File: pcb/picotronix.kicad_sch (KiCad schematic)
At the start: 25 parts, among them J1 Conn_02x04_Odd_Even, J2 Conn_02x04_Odd_Even, J3 DEBUG, J4 DB25_Male, U1 Pico, U2 TXS0104PW, U3 DAC7562SDGST, U4 TL074

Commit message: revised
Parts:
- removed C3, C4: C, Capacitor_SMD:C_0603_1608Metric_Pad1.08x0.95mm_HandSolder, symbol Device:C
- removed JP1: filter_bypass, Jumper:SolderJumper-2_P1.3mm_Open_Pad1.0x1.5mm, symbol Jumper:SolderJumper_2_Open
- removed R2, R3: R_US, Resistor_SMD:R_0603_1608Metric_Pad0.98x0.95mm_HandSolder, symbol Device:R_US
- removed RV1: Z Trim, Potentiometer_SMD:Potentiometer_Bourns_TC33X_Vertical, symbol Device:R_Potentiometer_Trim_US
- removed RV2: X Trim, Potentiometer_SMD:Potentiometer_Bourns_TC33X_Vertical, symbol Device:R_Potentiometer_Trim_US
- removed RV3: Y Trim, Potentiometer_SMD:Potentiometer_Bourns_TC33X_Vertical, symbol Device:R_Potentiometer_Trim_US
- removed U4: TL074, Package_SO:SOIC-14_3.9x8.7mm_P1.27mm, symbol Amplifier_Operational:TL074
- added R2: (no value), symbol Device:R
- added RN1, RN3: (no value), symbol Device:R_Pack04_Split
- added RN2: (no value), symbol Device:R_Pack04
- added RV1, RV2, RV3: (no value), symbol Device:R_Potentiometer_Trim
- added U4: (no value), symbol picotronix:ADA4891-3
- C1, C2, C5: value 0.1u -> (none); footprint Capacitor_SMD:C_0603_1608Metric_Pad1.08x0.95mm_HandSolder -> (none)
- C6: value 1u -> (none); footprint Capacitor_SMD:C_0603_1608Metric_Pad1.08x0.95mm_HandSolder -> (none)
- H1, H2, H3, H4: value MountingHole -> (none); footprint MountingHole:MountingHole_3.2mm_M3 -> (none)
- J1, J2: value Conn_02x04_Odd_Even -> (none); footprint Connector_PinSocket_2.54mm:PinSocket_2x04_P2.54mm_Vertical -> (none)
- J3: value DEBUG -> (none); footprint Connector_PinHeader_2.54mm:PinHeader_1x03_P2.54mm_Vertical -> (none)
- J4: value DB25_Male -> (none); footprint Connector_Dsub:DSUB-25_Male_Horizontal_P2.77x2.54mm_EdgePinOffset9.40mm -> (none)
- R1: value 10k -> (none); footprint Resistor_SMD:R_0603_1608Metric_Pad0.98x0.95mm_HandSolder -> (none); symbol Device:R_US -> Device:R
- U1: value Pico -> (none); footprint picotronix:RPi_Pico_SMD_TH -> (none)
- U2: value TXS0104PW -> (none); footprint Package_SO:TSSOP-14_4.4x5mm_P0.65mm -> (none); symbol picotronix:TXS0104PW -> picotronix:LSF0204DPWR; Digikey_PN (none) -> 296-40400-1-ND
- U3: value DAC7562SDGST -> (none); footprint Package_SO:VSSOP-10_3x3mm_P0.5mm -> (none); Digikey_PN (none) -> 296-38921-1-ND
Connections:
- net +5V: now also U4.4 (+V_{s})
- net GND: now also R2.1, RV3.3, U4.11 (-V_{s})
- net X_OUTPUT: now also RN2.1 (R1.1)
- net Y_OUTPUT: now also RN2.2 (R2.1)
- net Z_OUTPUT: now also RN2.3 (R3.1)
- net at U3.1 (V_{OUT}A): now also RV1.1
- net at U3.2 (V_{OUT}B): now also RV2.1
- net z_pwm: no longer names the net of U1.21 (GPIO16)
- new net: RN1.3 (R3.1), RN3.6 (R3.2), RN3.7 (R2.2)
- new net: RV2.2, U4.12 (+)
- new net: RN2.8 (R1.2), U4.13 (-), U4.15
- new net: RN2.6 (R3.2), U4.8, U4.9 (-)
- new net: RN2.7 (R2.2), U4.6 (-), U4.7
- new net: RN1.4 (R4.1), RN3.3 (R3.1), RV3.1
- new net: RN1.2 (R2.1), RN3.1 (R1.1), RN3.2 (R2.1)
- new net: R2.2, RN1.1 (R1.1), RN3.8 (R1.2)
- new net: RV3.2, U4.10 (+)
- new net: RV1.2, U4.5 (+)
- no-connect marks 20 -> 24
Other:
- note added: "extra gpio for later expansion"
- note added: "snub resistors to reduce peaking"
- note removed: "trim pots allow for ranging from 0-3.3v maximum."
- note removed: "z-axis pwm filter"
- moved on the sheet: C1, C2, C5, C6, J1, J2, U2

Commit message: update pcb
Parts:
- added TP? (x3): (no value), symbol Connector:TestPoint
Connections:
- net GND: now also RV1.3, RV2.3
- net X_OUTPUT: now also TP?.1
- net Y_OUTPUT: now also TP?.1
- net Z_OUTPUT: now also TP?.1
- net erase_interval_l: now also U1.32 (GPIO27_ADC1); no longer U1.31 (GPIO26_ADC0)
- net erase_l: now also U1.29 (GPIO22); no longer U1.27 (GPIO21)
- net non_store_l: now also U1.31 (GPIO26_ADC0); no longer U1.29 (GPIO22)
- net var_bright_l: now also U1.34 (GPIO28_ADC2); no longer U1.32 (GPIO27_ADC1)
- net ~{CS}: now also U1.27 (GPIO21); no longer U1.22 (GPIO17)
- net z_{3}: now reaches RN1.6 (R3.2)
- net z_{3}: now also U1.21 (GPIO16)
- net z_{1}: now reaches U1.19 (GPIO14)
- net z_{1}: now also RN1.8 (R1.2)
- net z_{2}: now reaches U1.20 (GPIO15)
- net z_{2}: now also RN1.7 (R2.2)
- net z_{4}: now reaches RN1.5 (R4.2)
- net z_{4}: now also U1.22 (GPIO17)
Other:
- note added: "r2r z-axis dac"
- moved on the sheet: RV1, RV2, U3, U4A, U4B

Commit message: update pcb
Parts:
- C1, C2, C5: value (none) -> 0.1u; footprint (none) -> Capacitor_SMD:C_0603_1608Metric_Pad1.08x0.95mm_HandSolder
- C6: value (none) -> 1u; footprint (none) -> Capacitor_SMD:C_0603_1608Metric_Pad1.08x0.95mm_HandSolder
- H1, H2, H3, H4: value (none) -> MountingHole; footprint (none) -> MountingHole:MountingHole_3.2mm_M3
- J1, J2: value (none) -> Conn_02x04_Odd_Even; footprint (none) -> Connector_PinSocket_2.54mm:PinSocket_2x04_P2.54mm_Vertical
- J3: value (none) -> DEBUG; footprint (none) -> Connector_PinHeader_2.54mm:PinHeader_1x03_P2.54mm_Vertical
- J4: value (none) -> DB25_Male; footprint (none) -> Connector_Dsub:DSUB-25_Male_Horizontal_P2.77x2.54mm_EdgePinOffset9.40mm
- R1, R2: value (none) -> 10k; footprint (none) -> Resistor_SMD:R_0603_1608Metric_Pad0.98x0.95mm_HandSolder
- RN1: value (none) -> 10k; footprint (none) -> Resistor_SMD:R_Array_Convex_4x1206
- RN2: value (none) -> 470; footprint (none) -> Resistor_SMD:R_Array_Convex_4x1206
- RN3: value (none) -> 4.99k; footprint (none) -> Resistor_SMD:R_Array_Convex_4x1206
- RV1, RV2, RV3: value (none) -> 20k; footprint (none) -> Potentiometer_SMD:Potentiometer_Bourns_TC33X_Vertical
- TP1: renamed from TP?; value (none) -> Z Test
- TP2: renamed from TP?; value (none) -> Y Test
- TP3: renamed from TP?; value (none) -> X test
- U1: value (none) -> Pico; footprint (none) -> picotronix:RPi_Pico_SMD_TH
- U2: value (none) -> LSF0204DPWR; footprint (none) -> Package_SO:TSSOP-14_4.4x5mm_P0.65mm
- U3: value (none) -> DAC7562SDGST; footprint (none) -> Package_SO:VSSOP-10_3x3mm_P0.5mm
- U4: value (none) -> ADA4891-3; footprint (none) -> Package_SO:TSSOP-14_4.4x5mm_P0.65mm

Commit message: pcb rev2 routed
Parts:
- removed J2: Conn_02x04_Odd_Even, Connector_PinSocket_2.54mm:PinSocket_2x04_P2.54mm_Vertical, symbol Connector_Generic:Conn_02x04_Odd_Even
- removed J3: DEBUG, Connector_PinHeader_2.54mm:PinHeader_1x03_P2.54mm_Vertical, symbol Connector:Conn_01x03_Male
- added C1, C10, C11, C2, C9: 0.1u, Capacitor_SMD:C_0603_1608Metric_Pad1.08x0.95mm_HandSolder, symbol Device:C_Small
- added C7, C8: 1u, Capacitor_SMD:C_0603_1608Metric_Pad1.08x0.95mm_HandSolder, symbol Device:C_Small
- added J1: AudioJack3_Ground, Connector_Audio:Jack_3.5mm_CUI_SJ-3524-SMT_Horizontal, symbol Connector:AudioJack3_Ground
- added J3: DEBUG, Connector_PinHeader_2.54mm:PinHeader_2x03_P2.54mm_Vertical, symbol Connector_Generic:Conn_02x03_Odd_Even
- added JP1: FMT_SET, Jumper:SolderJumper-2_P1.3mm_Open_TrianglePad1.0x1.5mm, symbol Jumper:SolderJumper_2_Open
- added JP2: MD1_SET, Jumper:SolderJumper-2_P1.3mm_Open_TrianglePad1.0x1.5mm, symbol Jumper:SolderJumper_2_Open
- added JP3: MD0_SET, Jumper:SolderJumper-2_P1.3mm_Open_TrianglePad1.0x1.5mm, symbol Jumper:SolderJumper_2_Open
- added R1: 10k, Resistor_SMD:R_0603_1608Metric_Pad0.98x0.95mm_HandSolder, symbol Device:R
- added SW1: BTN0, Button_Switch_SMD:SW_SPST_TL3305A, symbol Switch:SW_Push
- added SW2: BTN1, Button_Switch_SMD:SW_SPST_TL3305A, symbol Switch:SW_Push
- added SW3: RESET, Button_Switch_SMD:SW_SPST_TL3305A, symbol Switch:SW_Push
- added U5: W25Q128JVS, Package_SO:SOIC-8_5.23x5.23mm_P1.27mm, symbol Memory_Flash:W25Q128JVS
- added U6: PCM1808, Package_SO:TSSOP-14_4.4x5mm_P0.65mm, symbol picotronix:PCM1808
- J2: renamed from J1; value Conn_02x04_Odd_Even -> ESP-01 Connector
- J4: footprint Connector_Dsub:DSUB-25_Male_Horizontal_P2.77x2.54mm_EdgePinOffset9.40mm -> Connector_Dsub:DSUB-25_Male_Horizontal_P2.77x2.84mm_EdgePinOffset9.90mm_Housed_MountingHolesOffset11.32mm; symbol Connector:DB25_Male -> Connector:DB25_Male_MountingHoles
- TP1, TP2, TP3: footprint (none) -> TestPoint:TestPoint_Pad_2.0x2.0mm
- U3: value DAC7562SDGST -> AD5663R; footprint Package_SO:VSSOP-10_3x3mm_P0.5mm -> Package_SO:MSOP-10_3x3mm_P0.5mm; symbol picotronix:DAC7562SDGST -> picotronix:AD5663R; Digikey_PN 296-38921-1-ND -> AD5623RBRMZ-5REEL7CT-ND
- renumbered C1 to C3, C2 to C4, R1 to R2, R2 to R3, RN3 to RN2, RN2 to RN3, RV3 to RV1, RV1 to RV2, RV2 to RV3
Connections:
- net gpio6 is gone; now on net erase_interval_l: U1.9 (GPIO6)
- net gpio7 is gone; now on net erase_l: U1.10 (GPIO7)
- net +3V3: now also C1.1, C11.1, C9.1, JP1.2 (B), JP2.2 (B), JP3.2 (B), R1.1, U5.8 (VCC), U6.4 (V_{DD})
- net +5V: now also C10.1, U6.3 (V_{CC})
- net GND: now also J4.0 (PAD), C1.2, C10.2, C11.2, C2.2, C9.2, J1.G, J1.T, J3.5 (Pin_5), J3.6 (Pin_6), SW1.1, SW2.1, SW3.2, U5.4 (GND), U6.2 (AGND), U6.5 (DGND)
- net XY_FLUSH: now also U1.21 (GPIO16); no longer U1.26 (GPIO20)
- net erase_interval_l: no longer U1.32 (GPIO27_ADC1)
- net erase_l: no longer U1.29 (GPIO22)
- net non_store_l: now also U1.26 (GPIO20); no longer U1.31 (GPIO26_ADC0)
- net z_{1}: now also U1.16 (GPIO12); no longer U1.19 (GPIO14)
- net z_{2}: now also U1.17 (GPIO13); no longer U1.20 (GPIO15)
- net z_{3}: now also U1.19 (GPIO14); no longer U1.21 (GPIO16)
- net z_{4}: now also U1.20 (GPIO15); no longer U1.22 (GPIO17)
- net ~{CS}: now also U1.22 (GPIO17); no longer U1.27 (GPIO21)
- net at RN1.3 (R3.1), RN2.6 (R3.2): now also RN2.2 (R2.1); no longer RN2.7 (R2.2)
- net at RN1.2 (R2.1), RN2.1 (R1.1): now also RN2.7 (R2.2); no longer RN2.2 (R2.1)
- net at U1.30 (RUN): now also SW3.1
- net at U1.41 (SWCLK): now also J3.3 (Pin_3)
- net at U1.43 (SWDIO): now also J3.1 (Pin_1)
- net gpio0 renamed UART0_RX
- net UART0_RX: now also U1.2 (GPIO1); no longer U1.1 (GPIO0)
- net gpio1: no longer names the net of J2.3 (Pin_3)
- net gpio1: no longer U1.2 (GPIO1)
- net gpio10 renamed FLASH_SCK
- net FLASH_SCK: now also U5.6 (CLK)
- net gpio11 renamed FLASH_MOSI
- net FLASH_MOSI: now also U5.5 (DI(IO0))
- net gpio2: no longer names the net of U1.4 (GPIO2)
- net gpio2: now also SW1.2; no longer J2.4 (Pin_4)
- net gpio3: no longer names the net of J2.5 (Pin_5)
- net gpio3: no longer U1.5 (GPIO3)
- net gpio4: no longer names the net of J2.6 (Pin_6)
- net gpio4: no longer U1.6 (GPIO4)
- net gpio5 renamed UART0_TX
- net UART0_TX: now also U1.1 (GPIO0); no longer U1.7 (GPIO5)
- net gpio8 renamed FLASH_MISO
- net FLASH_MISO: now also U5.2 (DO(IO1))
- net gpio9 renamed FLASH_CS
- net FLASH_CS: now also U5.1 (~{CS})
- new net: JP2.1 (A), U6.11 (MD1)
- new net: JP3.1 (A), U6.10 (MD0)
- new net: SW2.2, U1.5 (GPIO3)
- new net: C2.1, U6.1 (V_{REF})
- new net: JP1.1 (A), U6.12 (FMT)
- new net: C7.1, U6.13 (V_{IN}L)
- new net: C8.1, U6.14 (V_{IN}R)
- new net: C7.2, J1.S
- new net: C8.2, J1.R
- new net dbg_rx: J3.2 (Pin_2), U1.7 (GPIO5)
- new net dbg_tx: J3.4 (Pin_4), U1.6 (GPIO4)
- new net esp_en: J2.4 (Pin_4), R1.2
- new net i2s_bck: U1.29 (GPIO22), U6.8 (BCK)
- new net i2s_dout: U1.31 (GPIO26_ADC0), U6.9 (DOUT)
- new net i2s_lrclk: U1.32 (GPIO27_ADC1), U6.7 (LRCK)
- new net i2s_mclk: U1.27 (GPIO21), U6.6 (SCKI)
- no-connect marks 24 -> 28
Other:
- note added: "audio input for reactive displays"
- note added: "esp-01 header for network connectivity"
- note added: "solder jumpers to set mode (internal pulldown)"
- note removed: "expansion ports are designed to be ESP-01 compatible"
- note removed: "extra gpio for later expansion"
- company: (none) -> Saji Champlin
- title: (none) -> Picotronix Main Board
- moved on the sheet: C3, C4, C5, C6, H1, H2, H3, H4, J2, R2, R3, RN1A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

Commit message: pcb final revision
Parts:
- removed R2: 10k, Resistor_SMD:R_0603_1608Metric_Pad0.98x0.95mm_HandSolder, symbol Device:R
- added R1: 10k, Resistor_SMD:R_0603_1608Metric_Pad0.98x0.95mm_HandSolder, symbol Device:R
- added TP10: ESP_BOOT, TestPoint:TestPoint_Pad_D1.0mm, symbol Connector:TestPoint
- added TP11: ESP_GPIO16, TestPoint:TestPoint_Pad_D1.0mm, symbol Connector:TestPoint
- added TP9: ESP_GPIO2, TestPoint:TestPoint_Pad_D1.0mm, symbol Connector:TestPoint
- C1: renamed from C8; Digikey_PN (none) -> 1276-1102-1-ND
- C10: renamed from C11; Digikey_PN (none) -> 1276-CL10B104KB8NNNLCT-ND
- C11: renamed from C1; Digikey_PN (none) -> 1276-CL10B104KB8NNNLCT-ND
- C2: renamed from C7; Digikey_PN (none) -> 1276-1102-1-ND
- C3: renamed from C2; Digikey_PN (none) -> 1276-CL10B104KB8NNNLCT-ND
- C4: renamed from C10; Digikey_PN (none) -> 1276-CL10B104KB8NNNLCT-ND
- C5: renamed from C9; Digikey_PN (none) -> 1276-CL10B104KB8NNNLCT-ND
- C6: renamed from C3; Digikey_PN (none) -> 1276-CL10B104KB8NNNLCT-ND
- C7: renamed from C4; Digikey_PN (none) -> 1276-CL10B104KB8NNNLCT-ND
- C8: renamed from C5; Digikey_PN (none) -> 1276-CL10B104KB8NNNLCT-ND
- C9: renamed from C6; Digikey_PN (none) -> 1276-1102-1-ND
- J1: Digikey_PN (none) -> CP-3524SJCT-ND
- J2: renamed from J3; Digikey_PN (none) -> S2011EC-03-ND
- J3: renamed from J4; Digikey_PN (none) -> AE10982-ND
- J4: renamed from J2; Digikey_PN (none) -> S7107-ND
- R2: renamed from R1; Digikey_PN (none) -> RNCP0603FTD10K0CT-ND
- R3: Digikey_PN (none) -> RNCP0603FTD10K0CT-ND
- SW1: renamed from SW3; Digikey_PN (none) -> EG5353CT-ND
- SW2: renamed from SW1; Digikey_PN (none) -> EG5353CT-ND
- SW3: renamed from SW2; Digikey_PN (none) -> EG5353CT-ND
- TP20: renamed from TP1; footprint TestPoint:TestPoint_Pad_2.0x2.0mm -> TestPoint:TestPoint_Pad_D1.0mm
- TP21: renamed from TP2; footprint TestPoint:TestPoint_Pad_2.0x2.0mm -> TestPoint:TestPoint_Pad_D1.0mm
- TP22: renamed from TP3; footprint TestPoint:TestPoint_Pad_2.0x2.0mm -> TestPoint:TestPoint_Pad_D1.0mm
- U1: renamed from U6; Digikey_PN (none) -> 296-19773-ND
- U3: renamed from U1; Digikey_PN (none) -> 2648-SC0915CT-ND
- U6: renamed from U5; Digikey_PN (none) -> W25Q128JVSIM-ND
- renumbered RN3 to RN1, RN1 to RN2, RN2 to RN3, RV3 to RV1, RV1 to RV3, U3 to U5
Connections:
- net +3V3: now also U2.8 (OE), R1.1
- net GND: no longer J1.G
- net at U4.12 (+): now also RV2.2; no longer RV1.2
- net at U4.6 (-), U4.7: now also RN1.8 (R1.2); no longer RN1.7 (R2.2)
- net esp_gpio2: now reaches J4.3 (Pin_3)
- net esp_gpio2: now also TP9.1
- net esp_boot: now reaches J4.5 (Pin_5)
- net esp_boot: now also TP10.1
- net esp_gpio16: now reaches J4.6 (Pin_6)
- net esp_gpio16: now also TP11.1
- net at U6.3 (IO2): now also U6.7 (IO3), R1.2
- net at U4.5 (+): now also RV1.2; no longer RV2.2
- new net: RN1.7 (R2.2), U4.13 (-), U4.14
- no-connect marks 28 -> 23
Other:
- moved on the sheet: C1, C10, C11, C2, C3, C4, C5, J1, J4, JP1, JP2, JP3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

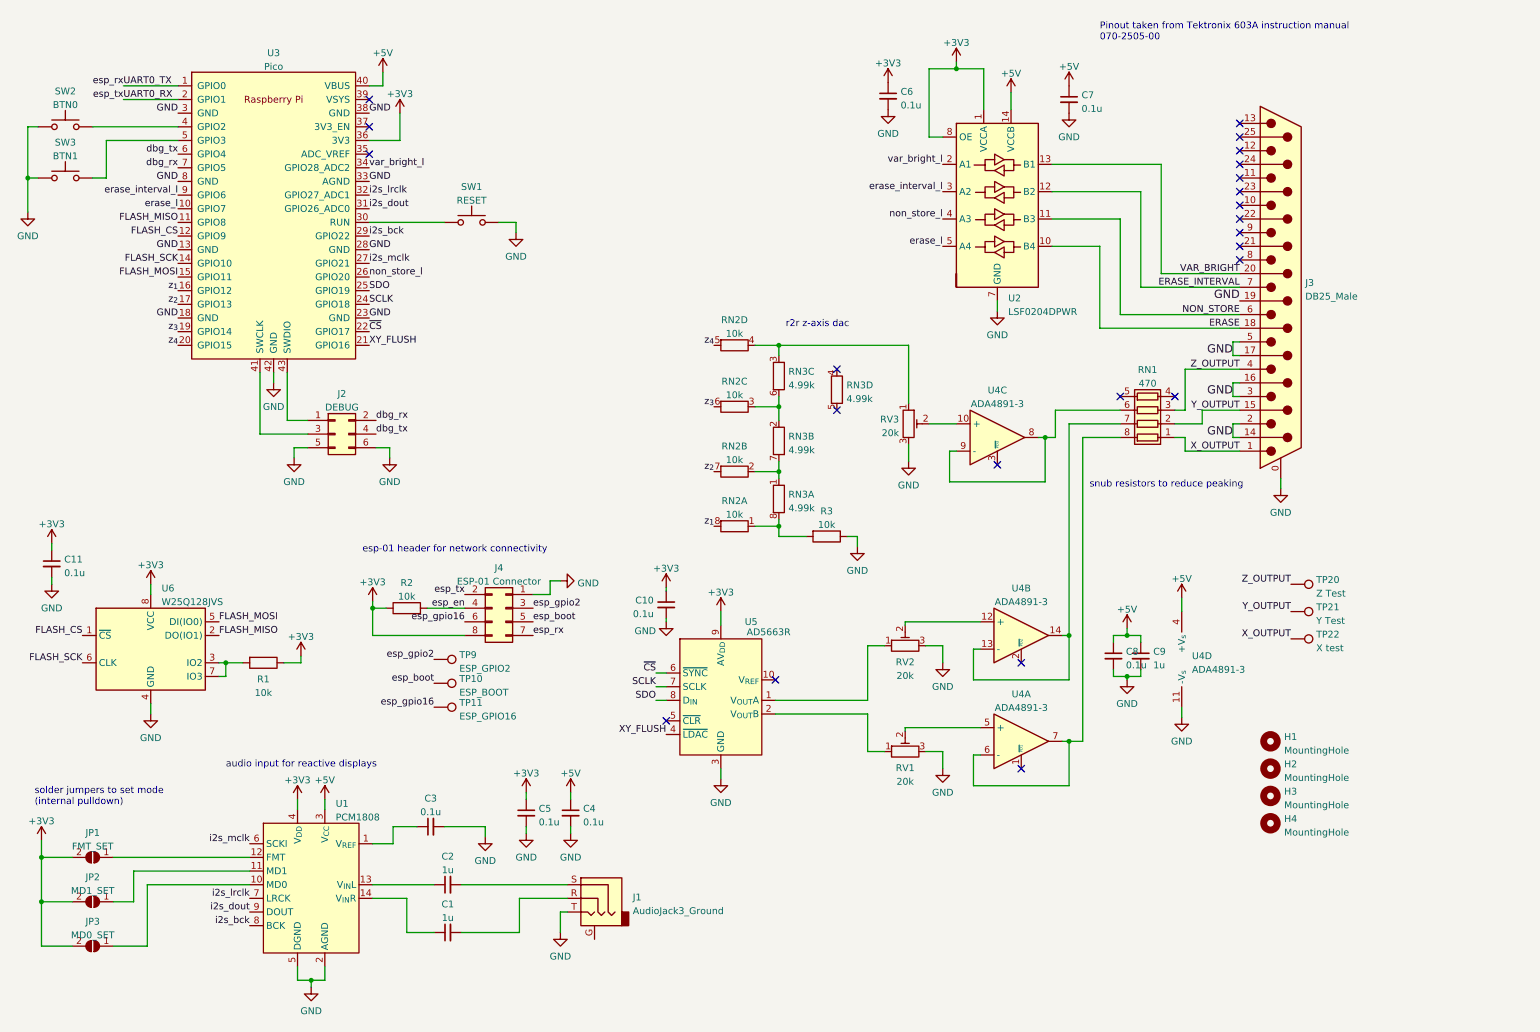
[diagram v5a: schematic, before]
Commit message: minor revisions to board and schematic (mostly cleanup)
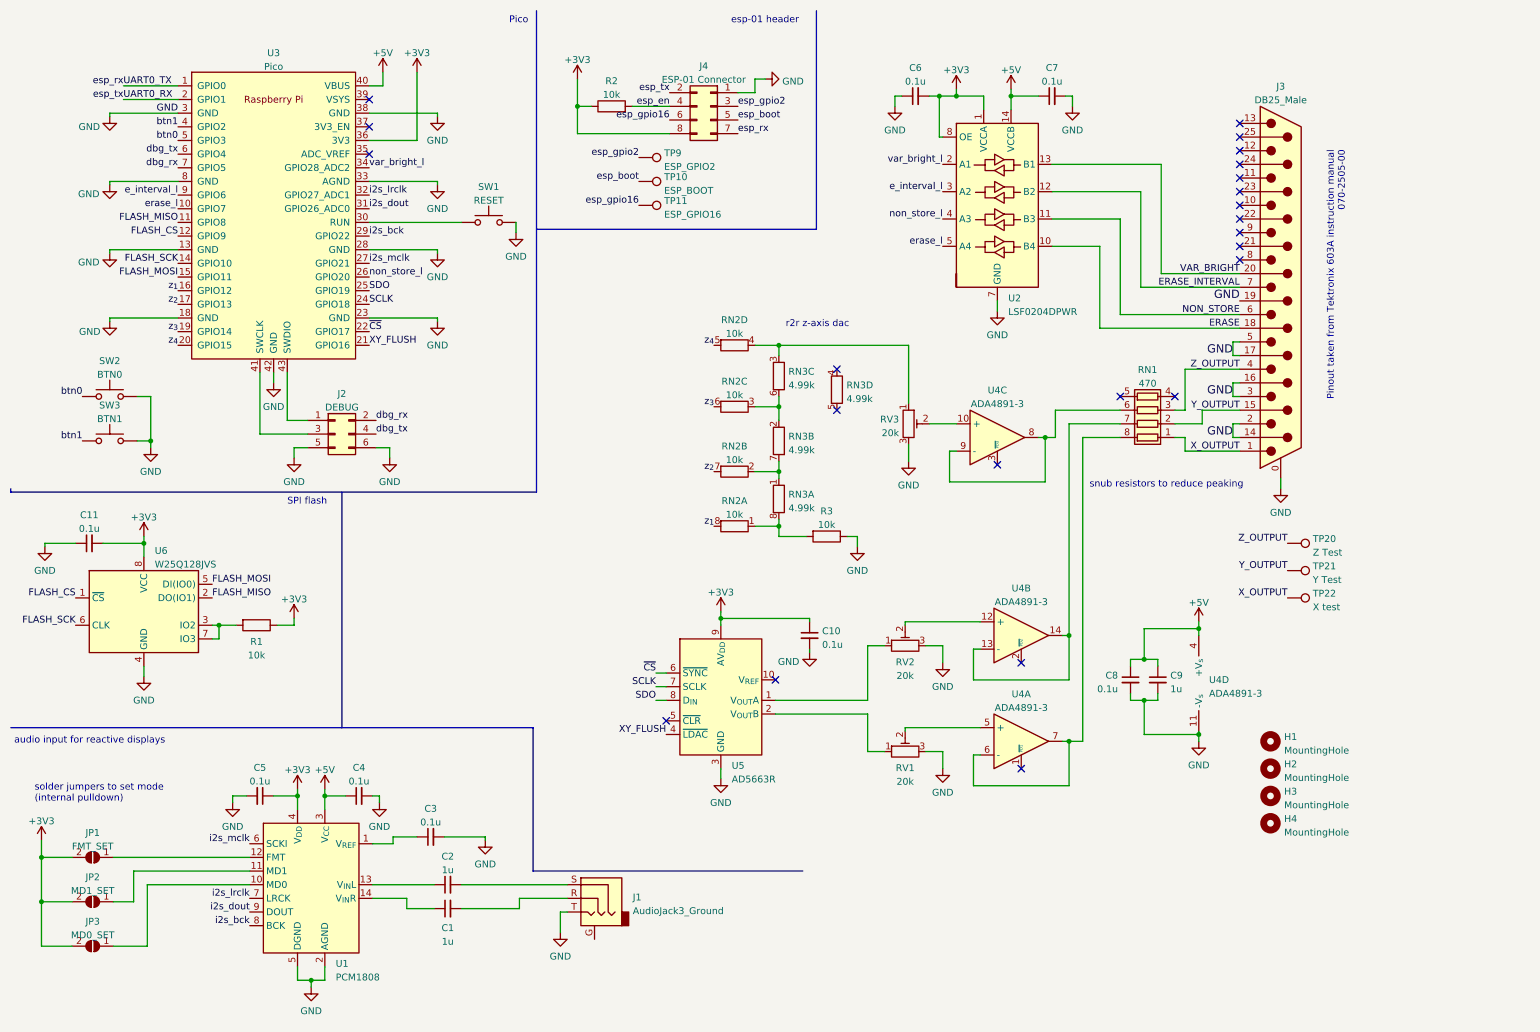
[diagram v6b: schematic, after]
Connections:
- net +3V3: now also C11.2, C6.2; no longer C11.1, C6.1
- net GND: now also C11.1, C6.1, SW2.2, SW3.2; no longer C11.2, C6.2, SW2.1, SW3.1
- net btn0: now reaches U3.5 (GPIO3)
- net btn0: now also SW2.1; no longer SW3.2
- net btn1: now reaches U3.4 (GPIO2)
- net btn1: now also SW3.1; no longer SW2.2
- net erase_interval_l renamed e_interval_l
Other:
- note added: "Pico"
- note added: "SPI flash"
- note added: "esp-01 header"
- note removed: "esp-01 header for network connectivity"
- moved on the sheet: C1, C10, C11, C3, C4, C5, C6, C7, C8, C9, J4, R1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
